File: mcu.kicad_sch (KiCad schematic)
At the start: 30 parts, among them U1 STM32H723VGTx, U13 BMI323, U14 AS5047P-ATST, U15 TCAN1044VDRQ1, X1 8MHz

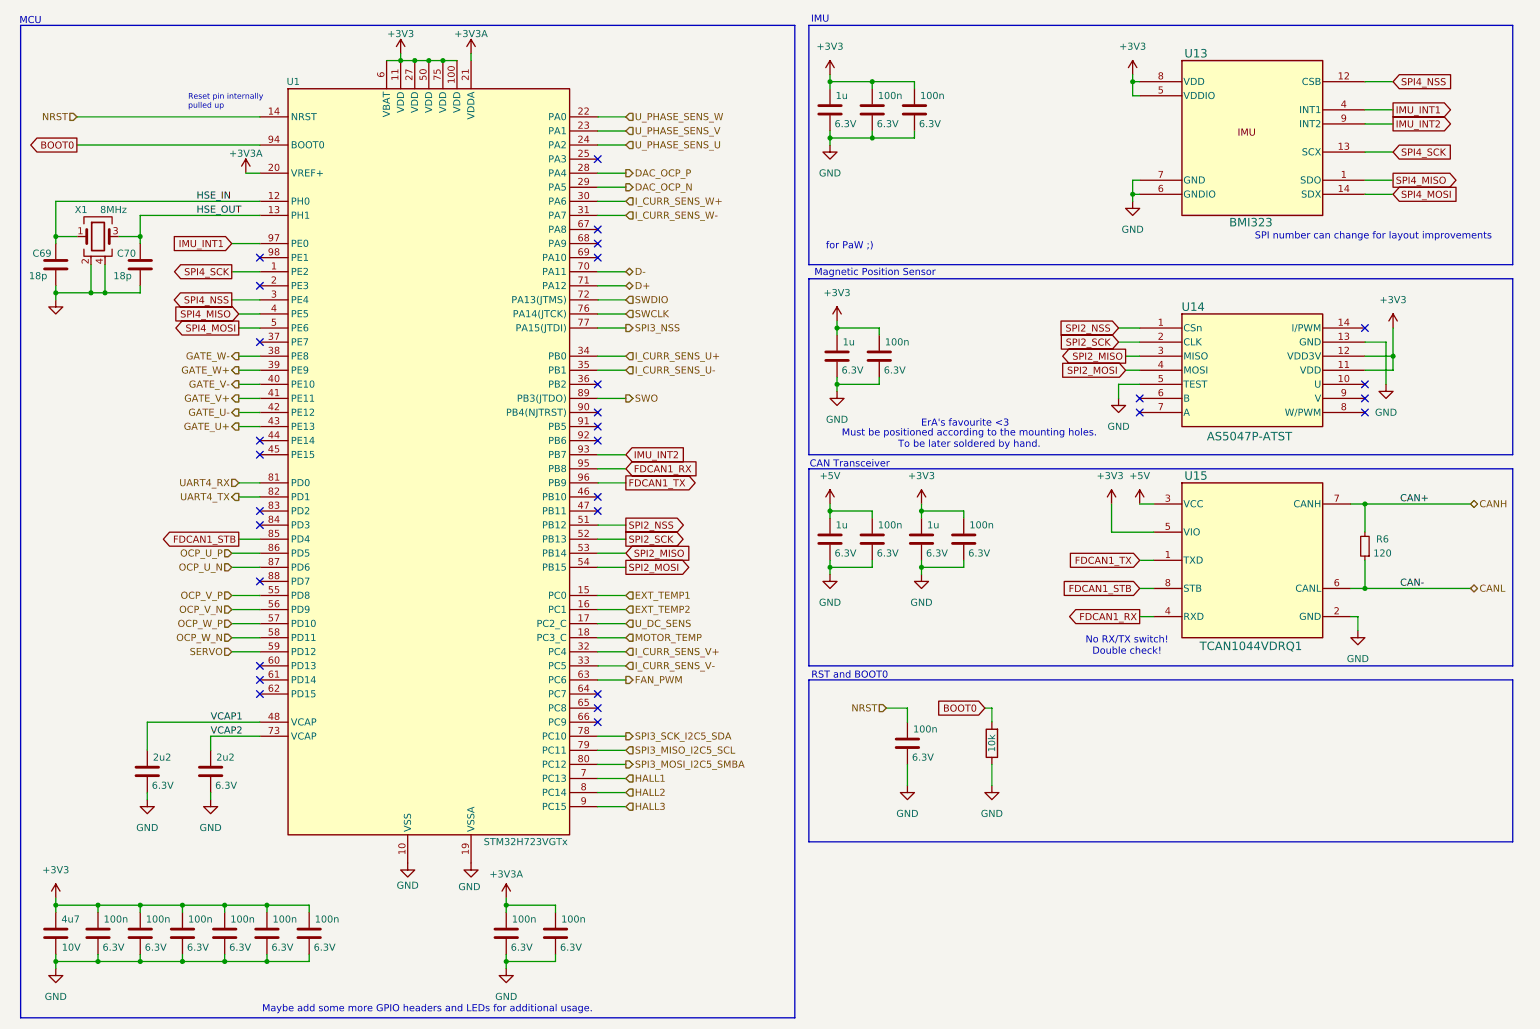
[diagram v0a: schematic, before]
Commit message: ERC errors have been fixed. XTAL changed to 12MHz. WiP DRC errors.
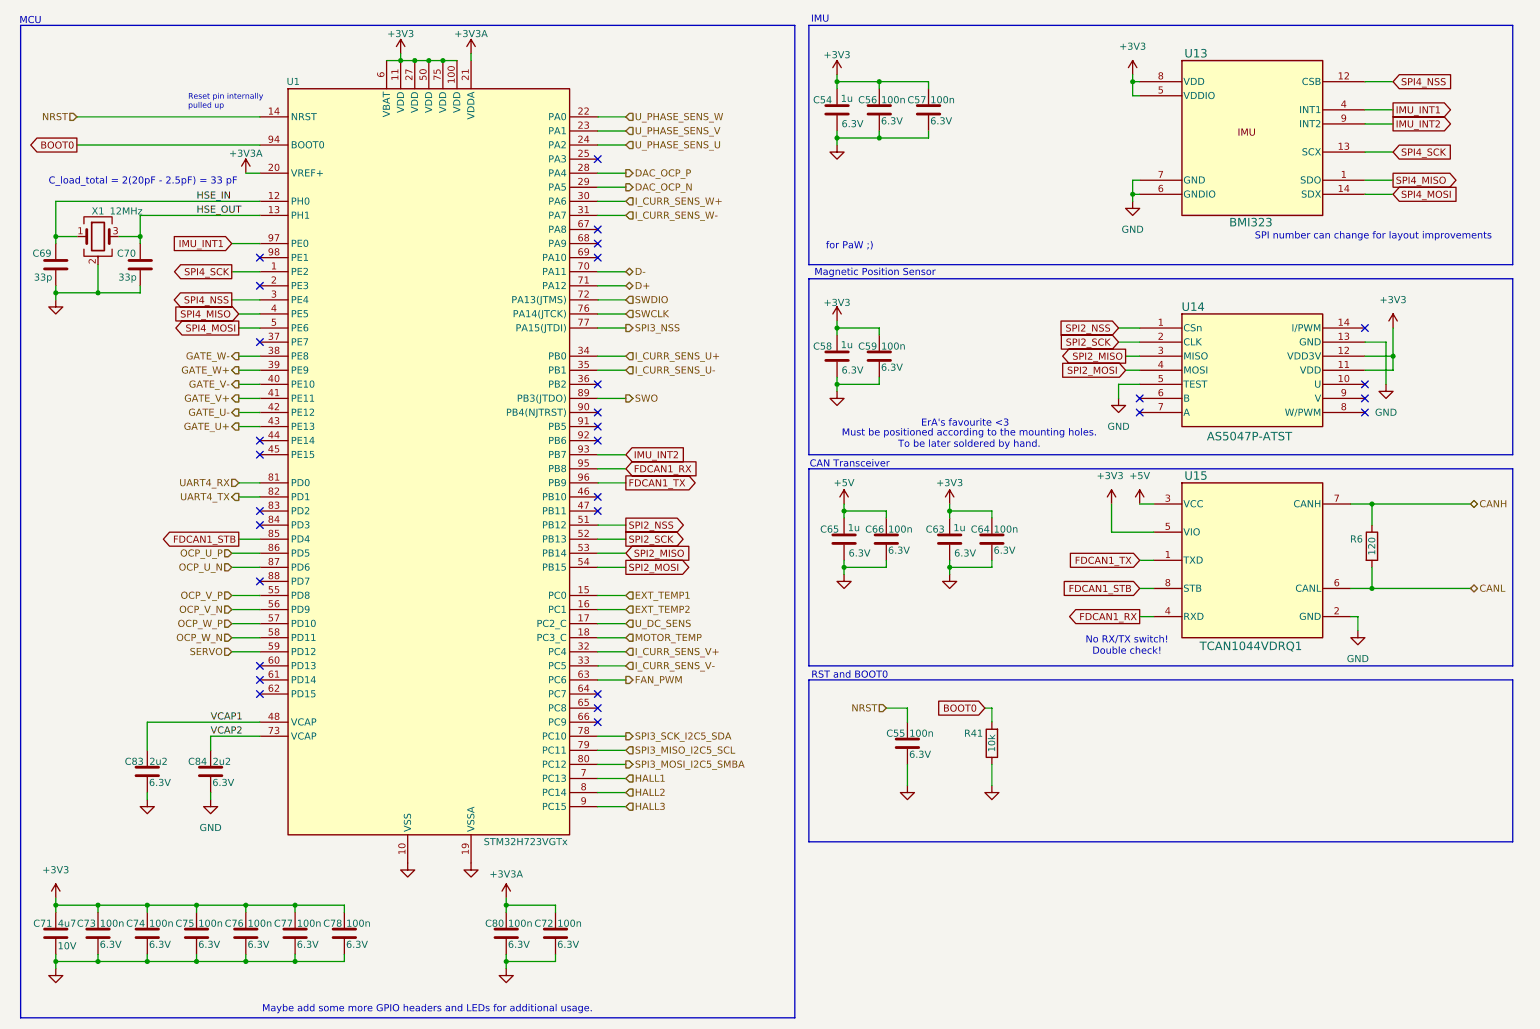
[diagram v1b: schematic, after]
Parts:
- removed R6: 120, Resistor_SMD:R_0402_1005Metric, symbol Device:R_Small
- added R6: 0402WGF1200TCE, Resistor_SMD:R_0402_1005Metric, symbol Device:R
- C54, C63, C65: value 1u -> CL05B105KQ5NQNC; Capacitance (none) -> 1u
- C55, C56, C57, C64, C66, C72, C73, C74, C75, C76, C77, C78, C80: value 100n -> 0402B104K6R3CT; Capacitance (none) -> 100n
- C58: value 1u -> ~; Capacitance (none) -> 1u
- C59: value 100n -> ~; Capacitance (none) -> 100n
- C69, C70: value 18p -> 0402CG330J500NT; Capacitance (none) -> 33p
- C71: value 4u7 -> CL05A475MP5NRNC; Capacitance (none) -> 4u7
- C83, C84: value 2u2 -> CL05A225MQ5NSNC; Capacitance (none) -> 2u2
- R41: value 10k -> 0402WGF1002TCE; Resistance (none) -> 10k
- U13: footprint BMI323_BOS -> NanoGaN:BMI323_BOS
- X1: value 8MHz -> X322512MSB4SI; Freq (none) -> 12MHz; LCSC C189764 -> (none)
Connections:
- net CANH: now also R6.1
- net CANL: now also R6.2
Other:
- note added: "C_load_total = 2(20pF - 2.5pF) = 33 pF"

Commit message: added leds and buttons
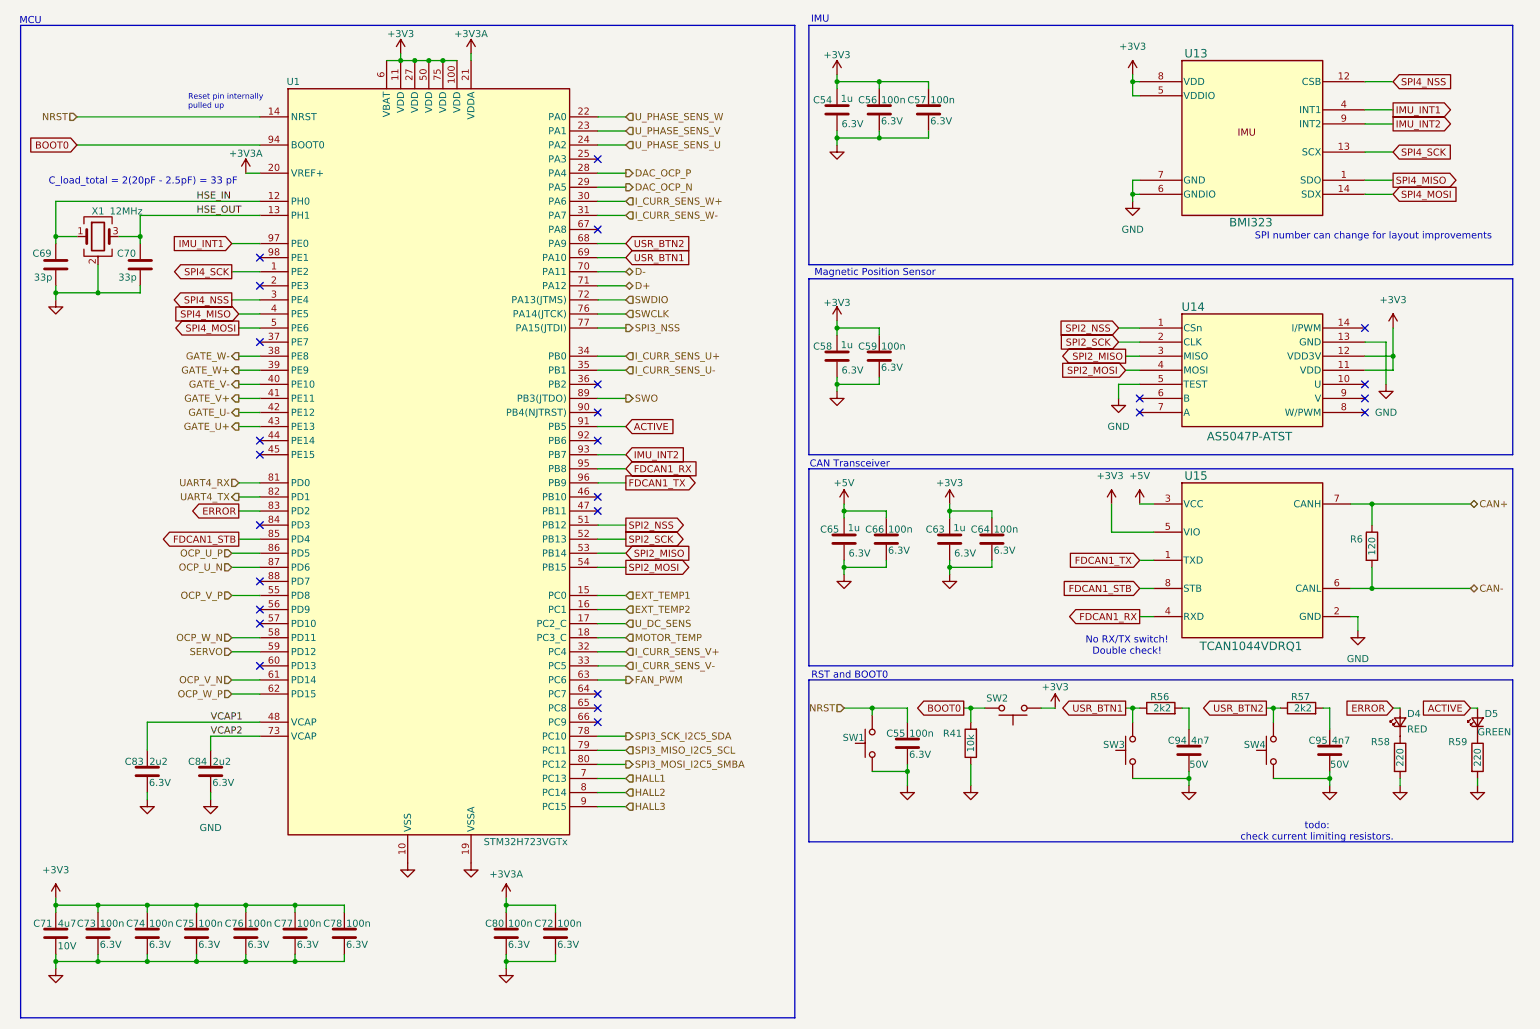
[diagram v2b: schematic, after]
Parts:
- added C94, C95: 0402B472K500NT, Capacitor_SMD:C_0402_1005Metric, symbol Device:C
- added D4: RED, LED_SMD:LED_0805_2012Metric, symbol Device:LED_Small
- added D5: GREEN, LED_SMD:LED_0805_2012Metric, symbol Device:LED_Small
- added R56, R57: 0402WGF1001TCE, Resistor_SMD:R_0402_1005Metric, symbol Device:R
- added R58, R59: 0402WGF2200TCE, Resistor_SMD:R_0402_1005Metric, symbol Device:R
- added SW1, SW2, SW3, SW4: TS-1088-AR02016, NanoGaN:SW_TS-1088_XNP, symbol Switch:SW_Push
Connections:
- net +3V3: now also SW2.1
- net BOOT0: now also SW2.2
- net GND: now also C94.2, C95.2, R58.2, R59.2, SW1.1, SW3.1, SW4.1
- net NRST: now also SW1.2
- net OCP_V_N: now also U1.61 (PD14); no longer U1.56 (PD9)
- net OCP_W_P: now also U1.62 (PD15); no longer U1.57 (PD10)
- net USR_BTN2: now reaches U1.68 (PA9)
- net USR_BTN2: now also R57.1, SW4.2
- net USR_BTN1: now reaches U1.69 (PA10)
- net USR_BTN1: now also R56.1, SW3.2
- net ERROR: now reaches U1.83 (PD2)
- net ERROR: now also D4.2 (A)
- net ACTIVE: now reaches U1.91 (PB5)
- net ACTIVE: now also D5.2 (A)
- net CANH renamed CAN+
- net CANL renamed CAN-
- new net: C94.1, R56.2
- new net: D4.1 (K), R58.1
- new net: D5.1 (K), R59.1
- new net: C95.1, R57.2
- no-connect marks 30 -> 26
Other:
- note added: "todo: check current limiting resistors."
- note removed: "ErA's favourite <3"
- note removed: "Maybe add some more GPIO headers and LEDs for additional usage."
- note removed: "Must be positioned according to the mounting holes. To be later soldered by hand."
- note removed: "for PaW ;)"
- moved on the sheet: R41

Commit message: schematic and PCB reviews are done, ready for release and first order.
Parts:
- R56, R57: value 0402WGF1001TCE -> 0402WGF2201TCE; LCSC C11702 -> C25879
- X1: LCSC (none) -> C9002
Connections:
- net OCP_U_N: now also U1.86 (PD5); no longer U1.87 (PD6)
- net OCP_U_P: now also U1.84 (PD3); no longer U1.86 (PD5)
- net OCP_V_N: now also U1.55 (PD8); no longer U1.61 (PD14)
- net OCP_V_P: now also U1.87 (PD6); no longer U1.55 (PD8)
- net OCP_W_N: now also U1.98 (PE1); no longer U1.58 (PD11)
- net OCP_W_P: now also U1.58 (PD11); no longer U1.62 (PD15)
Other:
- note removed: "todo: check current limiting resistors."
- company: (none) -> Eren Akbayin
- title: (none) -> NanoGaN

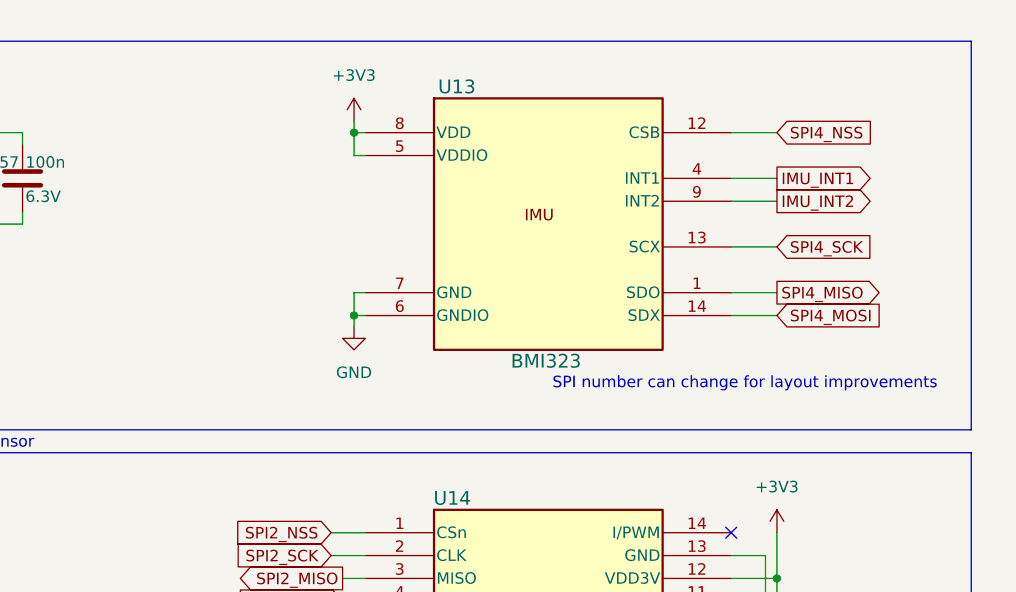
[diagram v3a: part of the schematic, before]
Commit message: changed the IMU from BMI323 to LSM6DSVTR
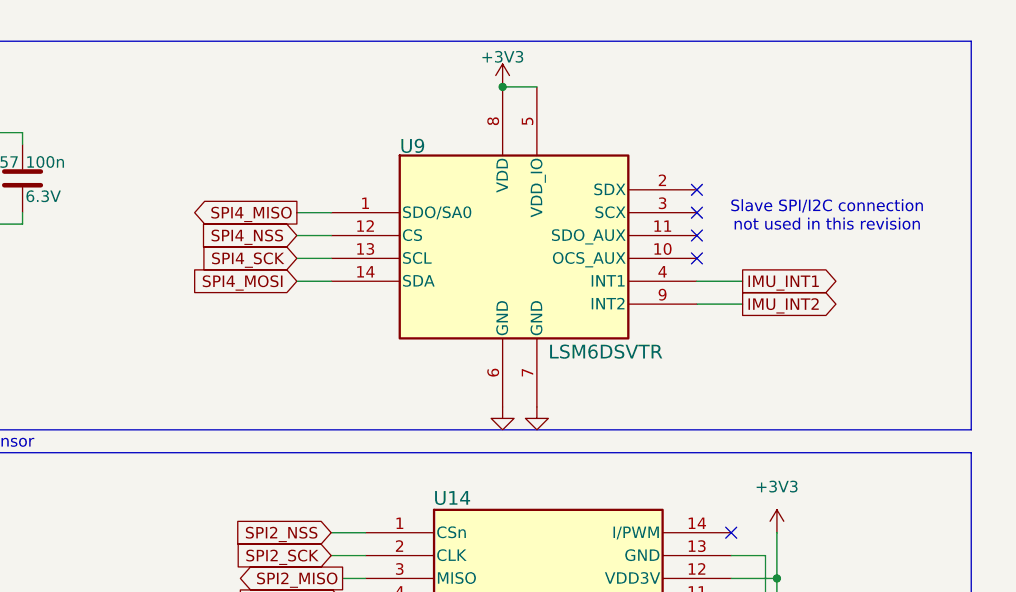
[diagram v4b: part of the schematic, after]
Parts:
- removed U13: BMI323, NanoGaN:BMI323_BOS, symbol NanoGaN:BMI323
- added U9: LSM6DSVTR, NanoGaN:LGA14-L_2P59X3P1X0P5_STM-L, symbol NanoGaN:LSM6DSVTR
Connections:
- net +3V3: now also U9.5 (VDD_IO), U9.8 (VDD)
- net GND: now also U9.6 (GND), U9.7 (GND)
- net IMU_INT1: now also U9.4 (INT1)
- net IMU_INT2: now also U9.9 (INT2)
- net SPI4_MISO: now also U9.1 (SDO/SA0)
- net SPI4_MOSI: now also U9.14 (SDA)
- net SPI4_NSS: now also U9.12 (CS)
- net SPI4_SCK: now also U9.13 (SCL)
- no-connect marks 26 -> 30
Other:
- note added: "Slave SPI/I2C connection not used in this revision"
- note removed: "SPI number can change for layout improvements"

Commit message: wip gate driver change
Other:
- moved on the sheet: U9
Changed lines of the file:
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@@
 	(text "Slave SPI/I2C connection\nnot used in this revision"
 		(exclude_from_sim no)
-		(at 265.938 34.798 0)
+		(at 269.494 34.544 0)
 		(effects
 			(font
@@
 	)
 	(junction
-		(at 229.87 20.32)
+		(at 233.68 20.32)
 		(diameter 0)
 		(color 0 0 0 0)
@@
 	)
 	(no_connect
-		(at 251.46 39.37)
+		(at 255.27 39.37)
 	)
 	(no_connect
-		(at 251.46 36.83)
+		(at 255.27 36.83)
 	)
 	(no_connect
@@
 	)
 	(no_connect
-		(at 251.46 31.75)
+		(at 255.27 31.75)
 	)
 	(no_connect
@@
 	)
 	(no_connect
-		(at 251.46 34.29)
+		(at 255.27 34.29)
 	)
 	(no_connect
@@
 	(wire
 		(pts
-			(xy 207.01 39.37) (xy 210.82 39.37)
+			(xy 210.82 39.37) (xy 214.63 39.37)
 		)
 		(stroke
@@
 	(wire
 		(pts
-			(xy 207.01 41.91) (xy 210.82 41.91)
+			(xy 210.82 41.91) (xy 214.63 41.91)
 		)
 		(stroke
@@
 	(wire
 		(pts
-			(xy 229.87 20.32) (xy 233.68 20.32)
+			(xy 233.68 20.32) (xy 237.49 20.32)
 		)
 		(stroke
@@
 	(wire
 		(pts
-			(xy 251.46 44.45) (xy 256.54 44.45)
+			(xy 255.27 44.45) (xy 260.35 44.45)
 		)
 		(stroke
@@
 	(wire
 		(pts
-			(xy 251.46 41.91) (xy 256.54 41.91)
+			(xy 255.27 41.91) (xy 260.35 41.91)
 		)
 		(stroke
@@
 	(wire
 		(pts
-			(xy 207.01 34.29) (xy 210.82 34.29)
+			(xy 210.82 34.29) (xy 214.63 34.29)
 		)
 		(stroke
@@
 	(wire
 		(pts
-			(xy 207.01 36.83) (xy 210.82 36.83)
+			(xy 210.82 36.83) (xy 214.63 36.83)
 		)
 		(stroke
@@
 	(global_label "SPI4_MOSI"
 		(shape input)
-		(at 207.01 41.91 180)
+		(at 210.82 41.91 180)
 		(fields_autoplaced yes)
 		(effects
@@
 		)
 		(property "Intersheetrefs" "${INTERSHEET_REFS}"
-			(at 194.1672 41.91 0)
+			(at 197.9772 41.91 0)
 			(effects
 				(font
@@
 	(global_label "IMU_INT2"
 		(shape output)
-		(at 256.54 44.45 0)
+		(at 260.35 44.45 0)
 		(fields_autoplaced yes)
 		(effects
@@
 		)
 		(property "Intersheetrefs" "${INTERSHEET_REFS}"
-			(at 267.9919 44.45 0)
+			(at 271.8019 44.45 0)
 			(effects
 				(font
@@
 	(global_label "SPI4_SCK"
 		(shape input)
-		(at 207.01 39.37 180)
+		(at 210.82 39.37 180)
 		(fields_autoplaced yes)
 		(effects
@@
 		)
 		(property "Intersheetrefs" "${INTERSHEET_REFS}"
-			(at 195.0139 39.37 0)
+			(at 198.8239 39.37 0)
 			(effects
 				(font
@@
 	(global_label "IMU_INT1"
 		(shape output)
-		(at 256.54 41.91 0)
+		(at 260.35 41.91 0)
 		(fields_autoplaced yes)
 		(effects
@@
 		)
 		(property "Intersheetrefs" "${INTERSHEET_REFS}"
-			(at 267.9919 41.91 0)
+			(at 271.8019 41.91 0)
 			(effects
 				(font
@@
 	(global_label "SPI4_MISO"
 		(shape output)
-		(at 207.01 34.29 180)
+		(at 210.82 34.29 180)
 		(fields_autoplaced yes)
 		(effects
@@
 		)
 		(property "Intersheetrefs" "${INTERSHEET_REFS}"
-			(at 194.1672 34.29 0)
+			(at 197.9772 34.29 0)
 			(effects
 				(font
@@
 	(global_label "SPI4_NSS"
 		(shape input)
-		(at 207.01 36.83 180)
+		(at 210.82 36.83 180)
 		(fields_autoplaced yes)
 		(effects
@@
 		)
 		(property "Intersheetrefs" "${INTERSHEET_REFS}"
-			(at 195.0139 36.83 0)
+			(at 198.8239 36.83 0)
 			(effects
 				(font
@@
 	(symbol
 		(lib_id "power:+3V3")
-		(at 229.87 20.32 0)
+		(at 233.68 20.32 0)
 		(unit 1)
 		(exclude_from_sim no)
@@
 		(dnp no)
 		(property "Reference" "#PWR0134"
-			(at 229.87 24.13 0)
+			(at 233.68 24.13 0)
 			(effects
 				(font
@@
 		)
 		(property "Value" "+3V3"
-			(at 229.87 17.018 0)
+			(at 233.68 17.018 0)
 			(effects
 				(font
@@
 		)
 		(property "Footprint" ""
-			(at 229.87 20.32 0)
+			(at 233.68 20.32 0)
 			(effects
 				(font
@@
 		)
 		(property "Datasheet" ""
-			(at 229.87 20.32 0)
+			(at 233.68 20.32 0)
 			(effects
 				(font
@@
 		)
 		(property "Description" "Power symbol creates a global label with name \"+3V3\""
-			(at 229.87 20.32 0)
+			(at 233.68 20.32 0)
 			(effects
 				(font
@@
 	(symbol
 		(lib_id "power:GND")
-		(at 229.87 55.88 0)
+		(at 233.68 55.88 0)
 		(unit 1)
 		(exclude_from_sim no)
@@
 		(fields_autoplaced yes)
 		(property "Reference" "#PWR082"
-			(at 229.87 62.23 0)
+			(at 233.68 62.23 0)
 			(effects
 				(font
@@
 		)
 		(property "Value" "GND"
-			(at 229.87 60.96 0)
+			(at 233.68 60.96 0)
 			(effects
 				(font
@@
 		)
 		(property "Footprint" ""
-			(at 229.87 55.88 0)
+			(at 233.68 55.88 0)
 			(effects
 				(font
@@
 		)
 		(property "Datasheet" ""
-			(at 229.87 55.88 0)
+			(at 233.68 55.88 0)
 			(effects
 				(font
@@
 		)
 		(property "Description" "Power symbol creates a global label with name \"GND\" , ground"
-			(at 229.87 55.88 0)
+			(at 233.68 55.88 0)
 			(effects
 				(font
@@
 	(symbol
 		(lib_id "NanoGaN:LSM6DSVTR")
-		(at 210.82 30.48 0)
+		(at 214.63 30.48 0)
 		(unit 1)
 		(exclude_from_sim no)
@@
 		(dnp no)
 		(property "Reference" "U9"
-			(at 218.44 26.924 0)
+			(at 222.25 26.924 0)
 			(effects
 				(font
@@
 		)
 		(property "Value" "LSM6DSVTR"
-			(at 234.95 49.784 0)
+			(at 238.76 49.784 0)
 			(effects
 				(font
@@
 		)
 		(property "Footprint" "NanoGaN:LGA14-L_2P59X3P1X0P5_STM-L"
-			(at 267.462 54.864 0)
+			(at 271.272 54.864 0)
 			(effects
 				(font
@@
 		)
 		(property "Datasheet" "LSM6DSVTR"
-			(at 258.572 56.896 0)
+			(at 262.382 56.896 0)
 			(effects
 				(font
@@
 		)
 		(property "Description" "-40℃~+85℃ 1.71V~3.6V 2.6uA 4.5KB IMU SPI、I2C、I3C X,Y,Z X,Y,Z ±16g ±4000dps LGA-14L(2.5x3) Accelerometers ROHS"
-			(at 307.086 59.436 0)
+			(at 310.896 59.436 0)
 			(effects
 				(font
@@
 		)
 		(property "LCSC" "C41785564"
-			(at 255.524 62.484 0)
+			(at 259.334 62.484 0)
 			(effects
 				(font
@@
 	(symbol
 		(lib_id "power:GND")
-		(at 233.68 55.88 0)
+		(at 237.49 55.88 0)
 		(unit 1)
 		(exclude_from_sim no)
@@
 		(fields_autoplaced yes)
 		(property "Reference" "#PWR0133"
-			(at 233.68 62.23 0)
+			(at 237.49 62.23 0)
 			(effects
 				(font
@@
 		)
 		(property "Value" "GND"
-			(at 233.68 60.96 0)
+			(at 237.49 60.96 0)
 			(effects
 				(font
@@
 		)
 		(property "Footprint" ""
-			(at 233.68 55.88 0)
+			(at 237.49 55.88 0)
 			(effects
 				(font
@@
 		)
 		(property "Datasheet" ""
-			(at 233.68 55.88 0)
+			(at 237.49 55.88 0)
 			(effects
 				(font
@@
 		)
 		(property "Description" "Power symbol creates a global label with name \"GND\" , ground"
-			(at 233.68 55.88 0)
+			(at 237.49 55.88 0)
 			(effects
 				(font
